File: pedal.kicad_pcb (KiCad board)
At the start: 2 copper layers, 29 parts, among them J2 USB_C_Receptacle_USB2.0_16P, U1 STM32H745XIH6, U2 TPS631000DRLR, U3 TLV77018PDBVR, U4 TPS2116DRL, U5 USBLC6-2SC6, U6 USBLC6-2SC6, U8 BQ27427YZFR

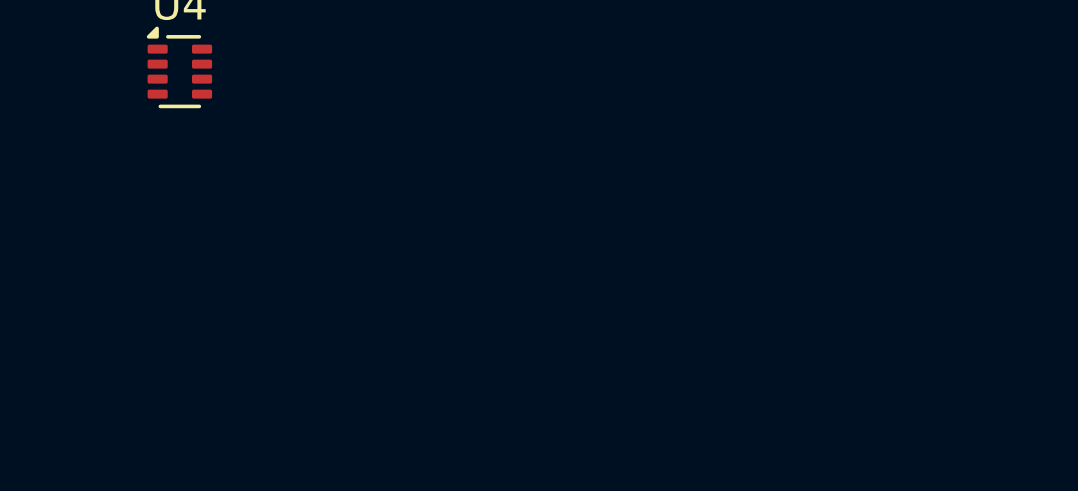
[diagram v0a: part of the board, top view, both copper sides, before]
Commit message: add switch model
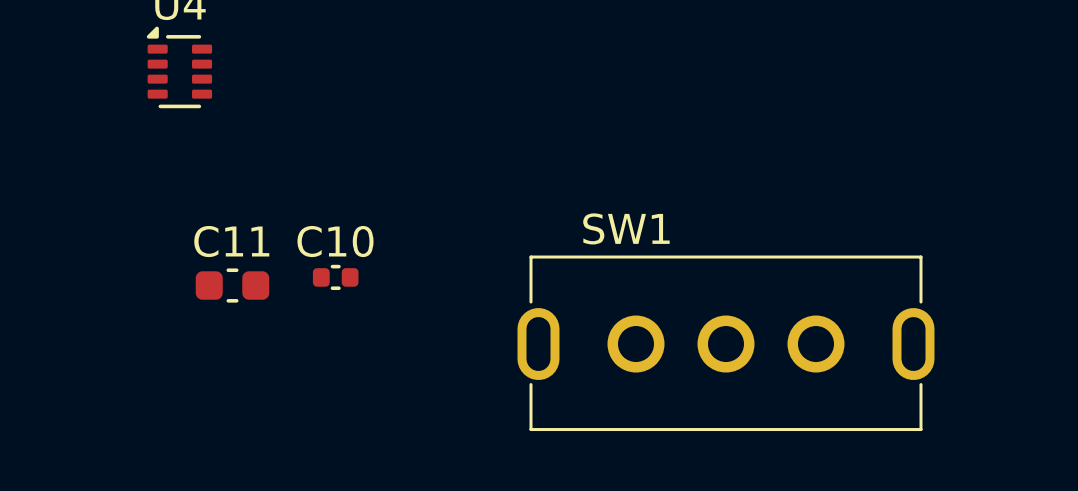
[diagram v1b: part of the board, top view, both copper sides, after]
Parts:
- added C10: 1uF, Capacitor_SMD:C_0402_1005Metric, F.Cu at (143.8, 145.6)
- added C11: 2.2uF, Capacitor_SMD:C_0603_1608Metric, F.Cu at (140.4, 145.9)
- added SW1: SW_SPST, footprints:SK-12E12-G060, F.Cu at (156.8, 147.8)
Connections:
- net /Power path/ICHG_B renamed /Power path/ICHG
- C9 pad 1: /Power path/VCELL -> Net-(SW1-A)
- L2 pad 2: /Power path/VCELL -> Net-(SW1-A)
- R9 pad 2: /Power path/ICHG_A -> GND
- U7 pad 10: /Power path/VCELL -> Net-(SW1-A)
- U8 pad A2: unconnected-(U8-SDA-PadA2) -> /Power path/SDA
- U8 pad A3: unconnected-(U8-SCL-PadA3) -> /Power path/SCL
- U8 pad B2: VSS -> GND
- U8 pad B3: unconnected-(U8-VDD-PadB3) -> Net-(U8-VDD)
- U8 pad C1: VSS -> GND
- U8 pad C2: unconnected-(U8-SRX-PadC2) -> Net-(SW1-A)
- U8 pad C3: unconnected-(U8-BAT-PadC3) -> Net-(BT1-+)

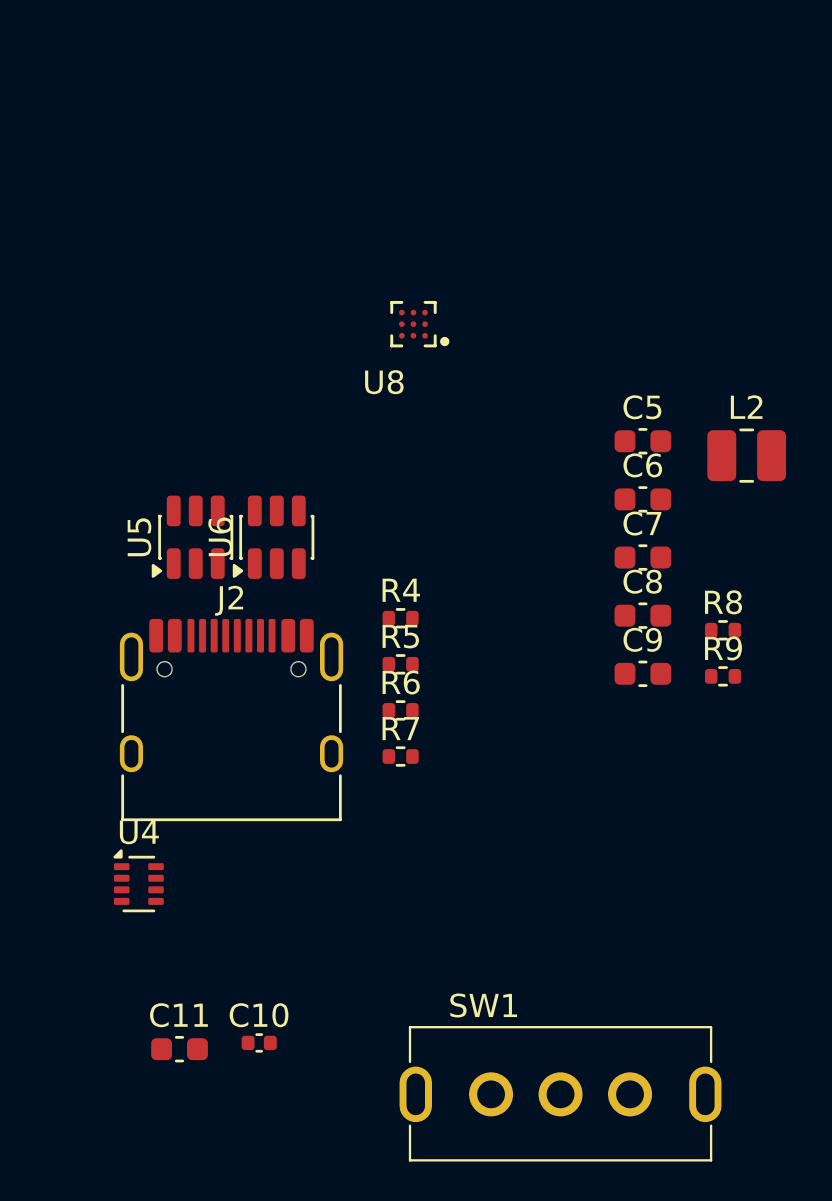
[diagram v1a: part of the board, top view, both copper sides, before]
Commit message: add pull up/down to fuel gauge
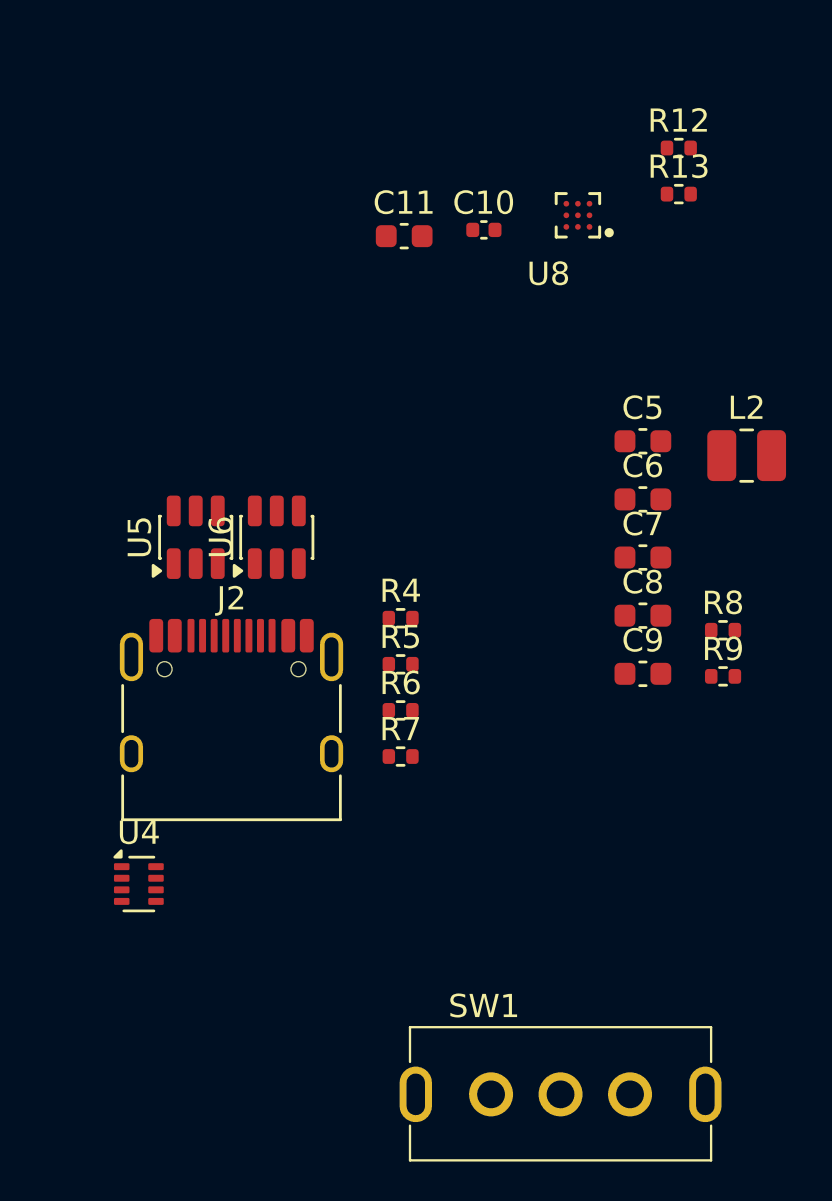
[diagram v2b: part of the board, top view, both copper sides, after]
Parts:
- added R12: 10k, Resistor_SMD:R_0402_1005Metric, F.Cu at (162.0, 107.0)
- added R13: 10k, Resistor_SMD:R_0402_1005Metric, F.Cu at (162.0, 109.0)
- U7: value ~ -> BQ25302
- moved C11 36.4 mm to (150.1, 110.8)
- moved C10 36.4 mm to (153.5, 110.5)
- moved U8 8.51 mm to (157.6, 109.9)
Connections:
- U8 pad A1: unconnected-(U8-GPOUT-PadA1) -> /Power path/GPOUT
- U8 pad B1: unconnected-(U8-BIN-PadB1) -> Net-(U8-BIN)

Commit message: LDO NC pin to ground
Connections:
- U3 pad 4: unconnected-(U3-NC-Pad4) -> GND
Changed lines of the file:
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@@
 			(layers "F.Cu" "F.Mask" "F.Paste")
 			(roundrect_rratio 0.25)
-			(net "unconnected-(U3-NC-Pad4)")
+			(net "GND")
 			(pinfunction "NC_4")
-			(pintype "no_connect")
+			(pintype "passive")
 		)
 		(pad "5" smd roundrect

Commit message: random changes
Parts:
- added REF**: ER-TFT023-1, footprints:ER-TFT023-1, F.Cu at (135.8, 122.7)
- SW1: value SW_SPST -> G-Switch SK-12E12-G060
- moved U7 76.9 mm to (180.0, 129.7)
- moved L2 18.0 mm to (181.9, 126.1)
- moved C9 9.65 mm to (169.6, 132.7), turned to 90 degrees
- moved C8 9.29 mm to (167.9, 132.7), turned to 90 degrees
- moved C7 9.28 mm to (168.8, 128.6)
- moved C5 9.28 mm to (168.8, 123.6)
- moved C6 9.28 mm to (168.8, 126.1)
- moved R8 9.04 mm to (172.9, 128.6)
- moved R9 9.01 mm to (172.9, 129.6)

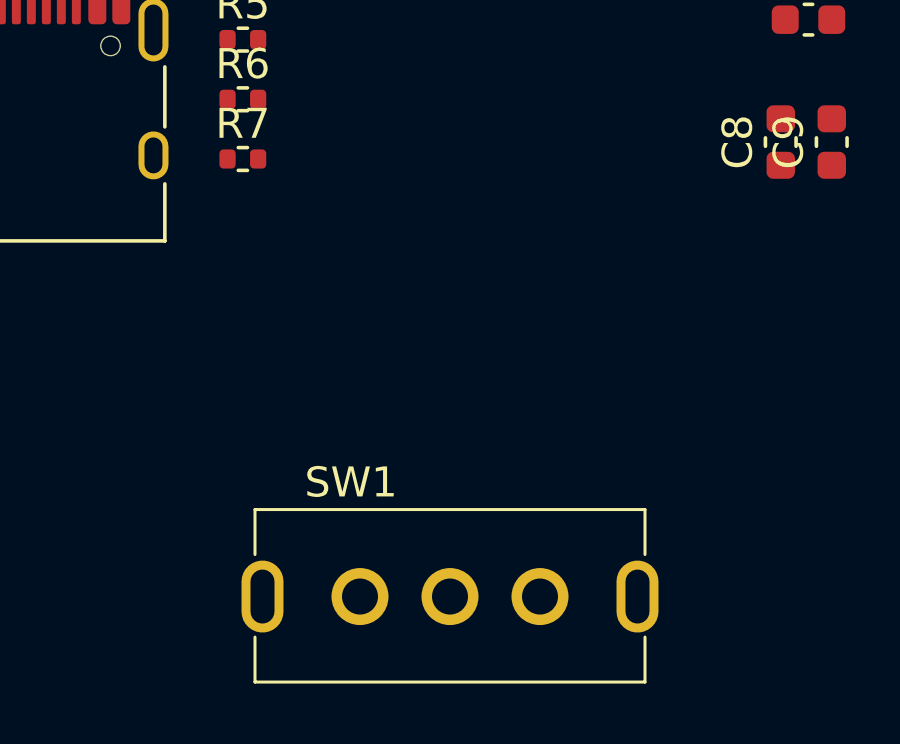
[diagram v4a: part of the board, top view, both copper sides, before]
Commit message: rename custom libraries to custom, add easyeda2kicad integration
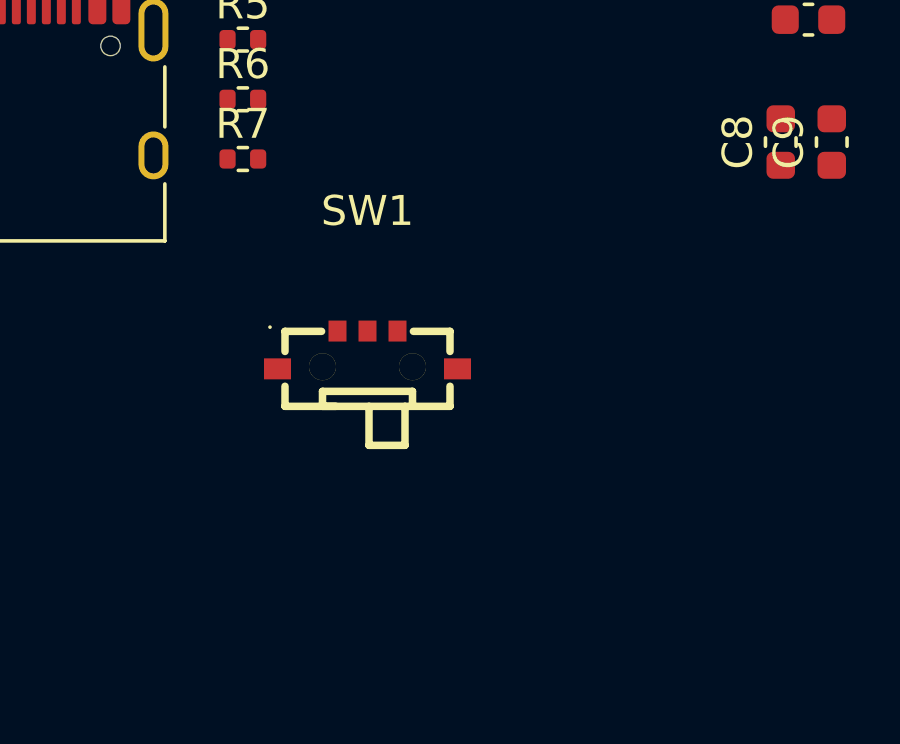
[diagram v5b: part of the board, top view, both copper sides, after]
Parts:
- SW1: value G-Switch SK-12E12-G060 -> MK-11C04-G013; footprint footprints:SK-12E12-G060 -> custom:SW-SMD_MK-11C04-G013
- moved SW1 8.67 mm to (154.1, 139.6)
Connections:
- C9 pad 1: Net-(SW1-A) -> Net-(U7-BAT)
- L2 pad 2: Net-(SW1-A) -> Net-(U7-BAT)
- SW1 pad 1: Net-(SW1-A) -> /Power path/VBATT
- SW1 pad 2: /Power path/VBATT -> unconnected-(SW1-Pad2)
- U7 pad 10: Net-(SW1-A) -> Net-(U7-BAT)
- U8 pad C2: Net-(SW1-A) -> Net-(U7-BAT)

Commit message: embed all 3d models
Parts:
- moved REF** 49.8 mm to (86.0, 120.8)

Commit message: move stuff a bit
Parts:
- moved U1 5.73 mm to (124.7, 113.3)
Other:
- copper layers 2 -> 4
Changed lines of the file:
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@@
 	(layers
 		(0 "F.Cu" signal)
+		(4 "In1.Cu" signal)
+		(6 "In2.Cu" signal)
 		(2 "B.Cu" signal)
 		(9 "F.Adhes" user "F.Adhesive")
@@
 	)
 	(setup
+		(stackup
+			(layer "F.SilkS"
+				(type "Top Silk Screen")
+			)
+			(layer "F.Paste"
+				(type "Top Solder Paste")
+			)
+			(layer "F.Mask"
+				(type "Top Solder Mask")
+				(thickness 0.01)
+			)
+			(layer "F.Cu"
+				(type "copper")
+				(thickness 0.035)
+			)
+			(layer "dielectric 1"
+				(type "prepreg")
+				(thickness 0.1)
+				(material "FR4")
+				(epsilon_r 4.5)
+				(loss_tangent 0.02)
+			)
+			(layer "In1.Cu"
+				(type "copper")
+				(thickness 0.035)
+			)
+			(layer "dielectric 2"
+				(type "core")
+				(thickness 1.24)
+				(material "FR4")
+				(epsilon_r 4.5)
+				(loss_tangent 0.02)
+			)
+			(layer "In2.Cu"
+				(type "copper")
+				(thickness 0.035)
+			)
+			(layer "dielectric 3"
+				(type "prepreg")
+				(thickness 0.1)
+				(material "FR4")
+				(epsilon_r 4.5)
+				(loss_tangent 0.02)
+			)
+			(layer "B.Cu"
+				(type "copper")
+				(thickness 0.035)
+			)
+			(layer "B.Mask"
+				(type "Bottom Solder Mask")
+				(thickness 0.01)
+			)
+			(layer "B.Paste"
+				(type "Bottom Solder Paste")
+			)
+			(layer "B.SilkS"
+				(type "Bottom Silk Screen")
+			)
+			(copper_finish "None")
+			(dielectric_constraints no)
+		)
 		(pad_to_mask_clearance 0)
 		(allow_soldermask_bridges_in_footprints no)
@@
 		(capping no)
 		(filling no)
+		(zone_defaults)
 		(pcbplotparams
 			(layerselection 0x00000000_00000000_55555555_5755f5ff)
@@
 	(footprint "footprints:BGA265C80P17X17_1400X1400X120"
 		(layer "F.Cu")
-		(at 119.025 112.525)
+		(at 124.7 113.3)
 		(property "Reference" "U1"
 			(at -3.825 -8.885 0)

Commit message: update pcb
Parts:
- added JP1: ~, Jumper:SolderJumper-2_P1.3mm_Bridged2Bar_RoundedPad1.0x1.5mm, F.Cu at (188.8, 133.1)
- added R10: 4.53k, Resistor_SMD:R_0402_1005Metric, F.Cu at (185.6, 126.5)
- added R11: 23.2k, Resistor_SMD:R_0402_1005Metric, F.Cu at (185.1, 134.3)
- added R14: 10k, Resistor_SMD:R_0402_1005Metric, F.Cu at (185.1, 136.3)
- R8: value 27k -> 22k
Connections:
- net Net-(BT1-+) renamed /Power path/VBATT_RAW
- SW1 pad 1: /Power path/VBATT -> unconnected-(SW1-Pad1)
- SW1 pad 2: unconnected-(SW1-Pad2) -> Net-(U7-BAT)
- SW1 pad C: Net-(U7-BAT) -> /Power path/VBATT
